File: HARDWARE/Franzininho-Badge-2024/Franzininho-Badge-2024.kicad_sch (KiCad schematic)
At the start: 15 parts, among them SW1 SW_Push, U1 CH32V003F4P6

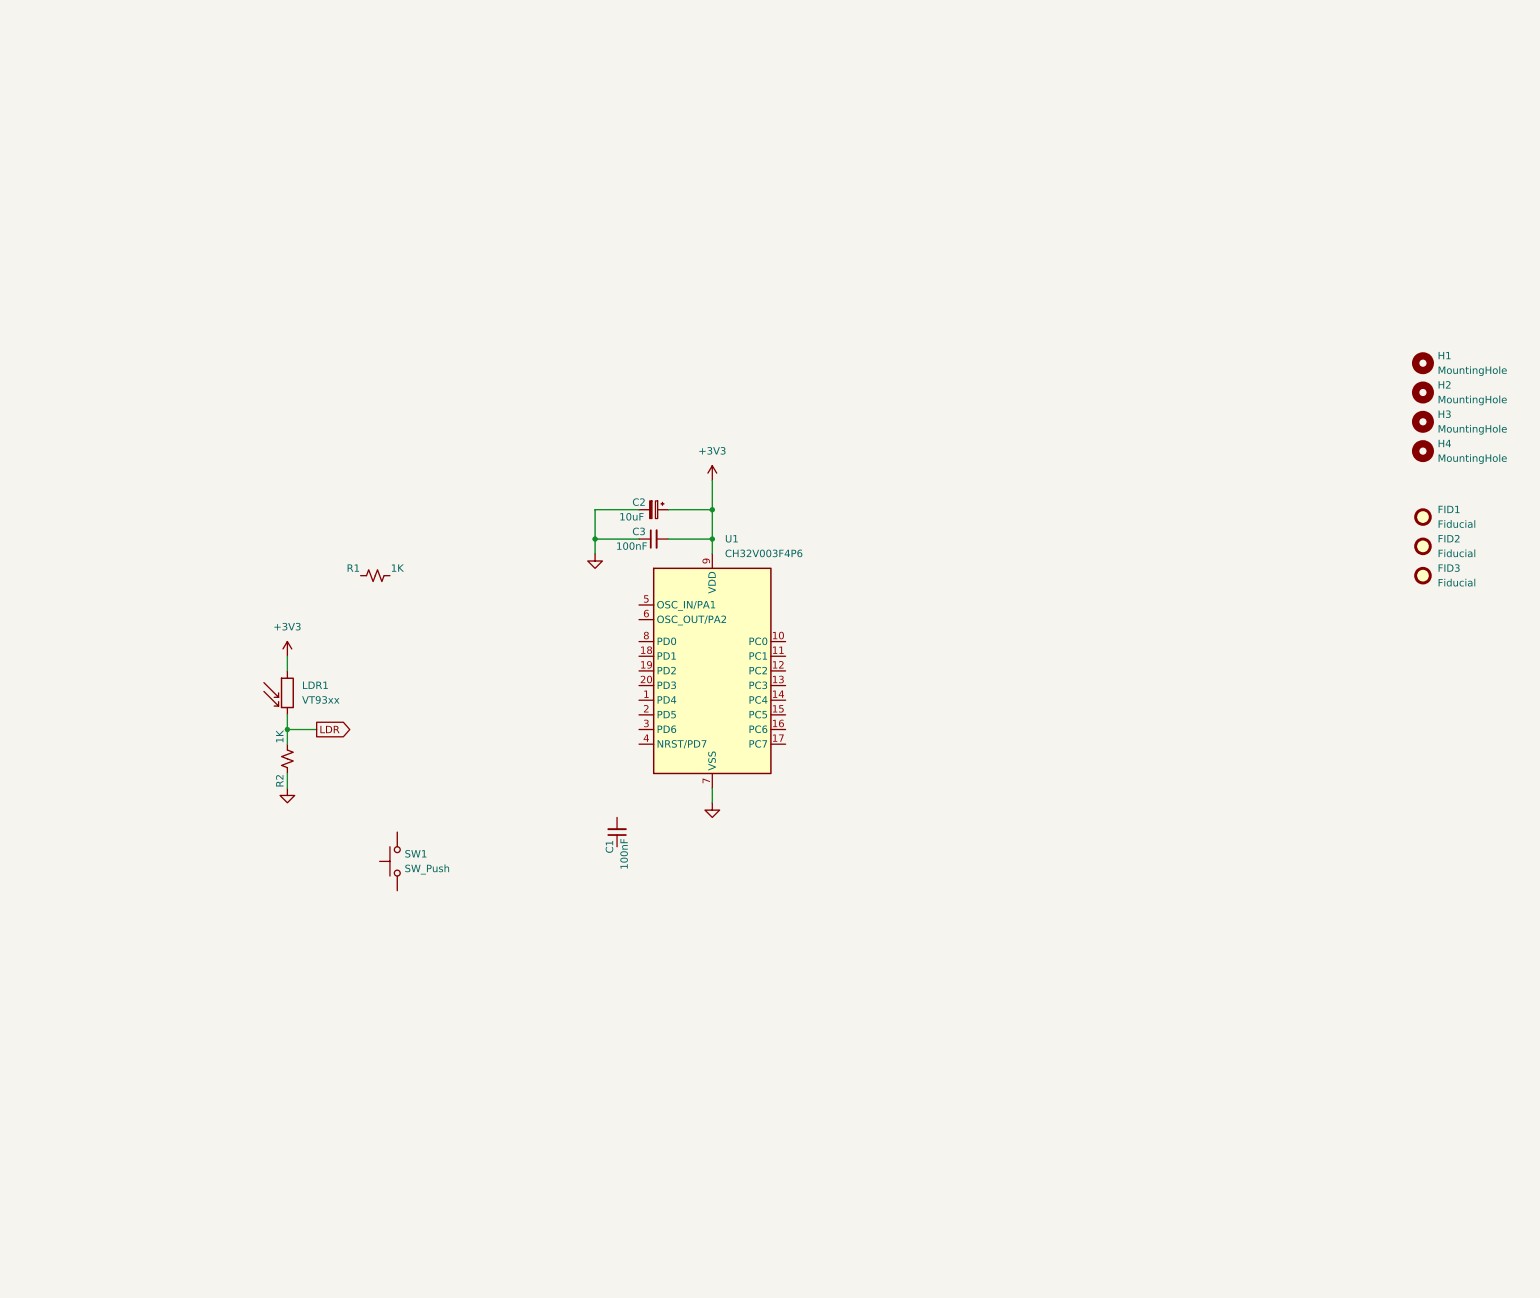
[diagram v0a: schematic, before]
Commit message: Adicionando displays.
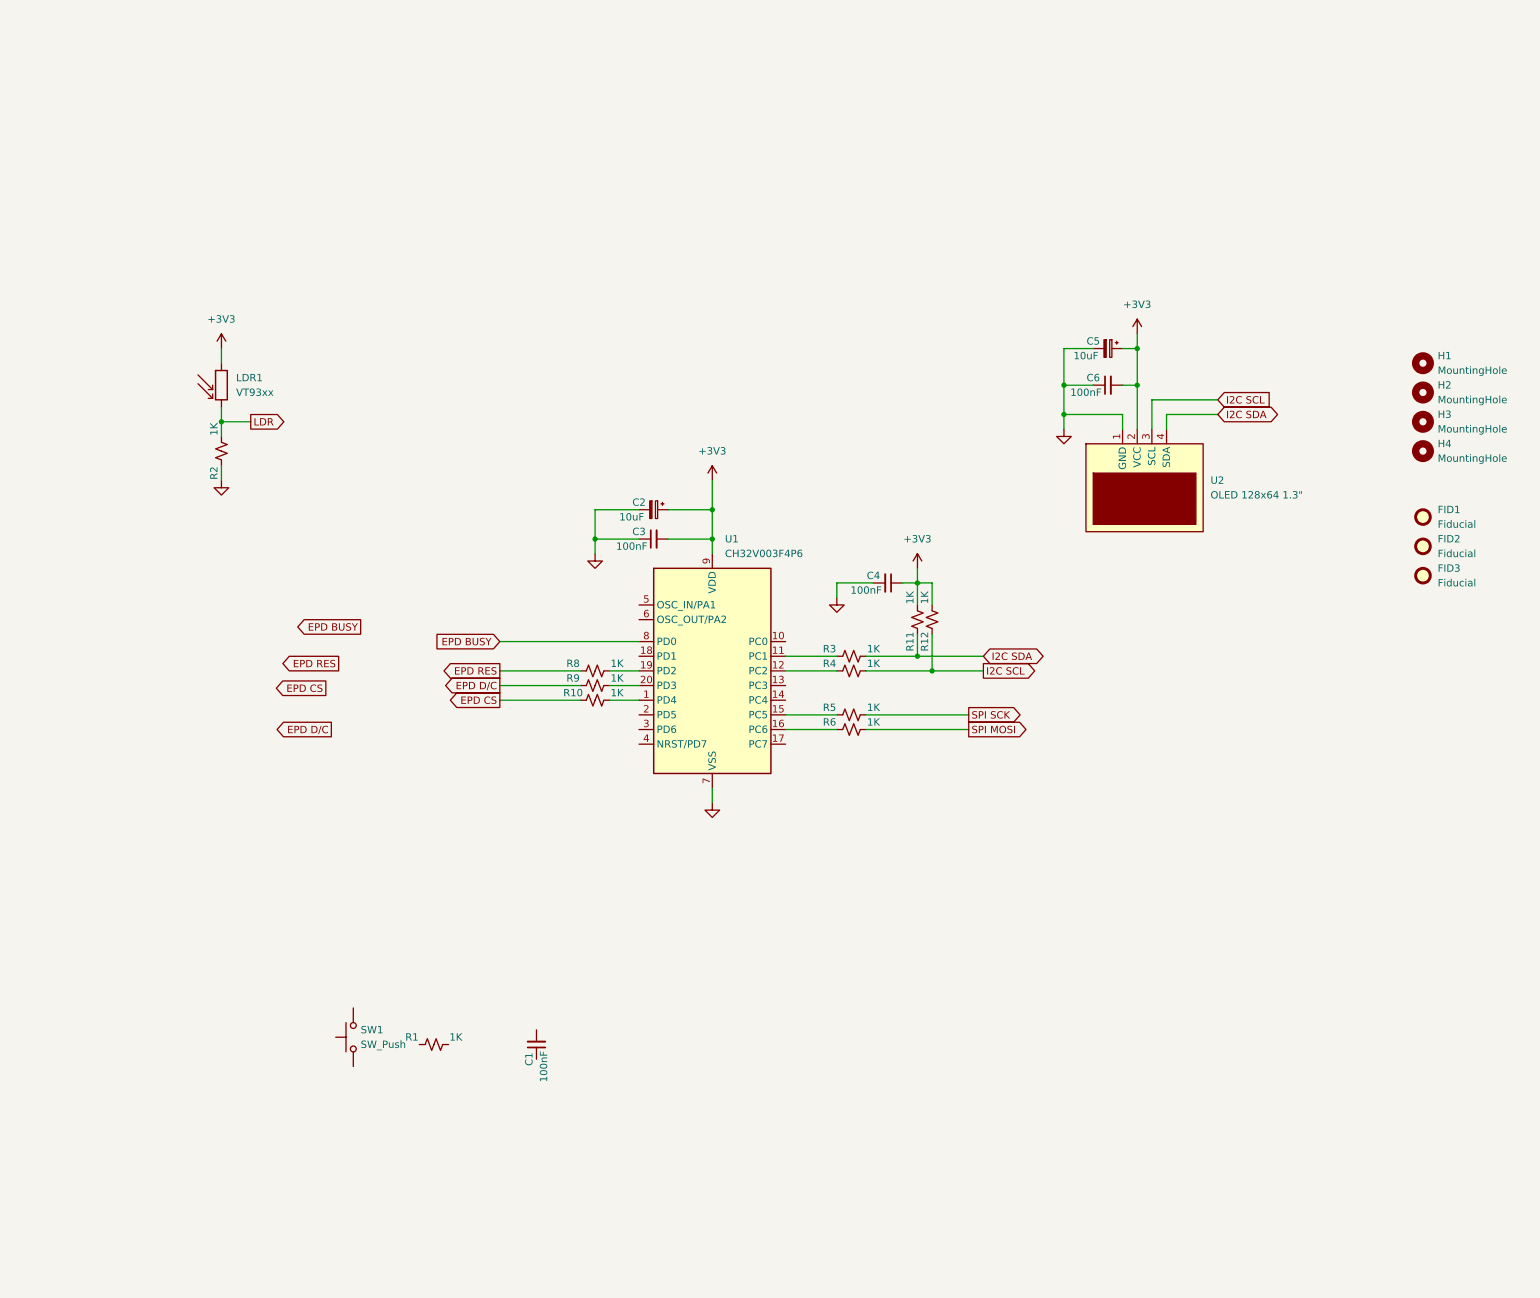
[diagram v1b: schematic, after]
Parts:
- added C4, C6: 100nF, Capacitor_SMD:C_0603_1608Metric_Pad1.08x0.95mm_HandSolder, symbol Device:C_Small
- added C5: 10uF, Capacitor_SMD:C_0805_2012Metric_Pad1.18x1.45mm_HandSolder, symbol Device:C_Polarized_Small
- added R10, R11, R12, R3, R4, R5, R6, R8, R9: 1K, Resistor_SMD:R_0603_1608Metric_Pad0.98x0.95mm_HandSolder, symbol Device:R_Small_US
- added U2: OLED 128x64 1.3", Franzininho-Badge:OLED 128x64 1.3in, symbol Franzininho-Badge:OLED_128x64_1.3{dblquote}
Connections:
- net +3V3: now also C4.1, C5.1, C6.2, R11.2, R12.2, U2.2 (VCC)
- net GND: now also C4.2, C5.2, C6.1, U2.1 (GND)
- net at U1.1 (PD4): now also R10.2
- net at U1.11 (PC1): now also R3.1
- net at U1.12 (PC2): now also R4.1
- net at U1.15 (PC5): now also R5.1
- net at U1.16 (PC6): now also R6.1
- net at U1.19 (PD2): now also R8.2
- net at U1.20 (PD3): now also R9.2
- net EPD BUSY: now reaches U1.8 (PD0)
- new net EPD CS: R10.1
- new net EPD D/C: R9.1
- new net EPD RES: R8.1
- new net I2C SCL: R12.1, R4.2, U2.3 (SCL)
- new net I2C SDA: R11.1, R3.2, U2.4 (SDA)
- new net SPI MOSI: R6.2
- new net SPI SCK: R5.2
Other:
- moved on the sheet: C1, LDR1, R1, R2, SW1

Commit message: Esboço inicial do layout.
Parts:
- added J1: Conn_01x03_Pin, Connector_PinHeader_2.54mm:PinHeader_1x03_P2.54mm_Horizontal, symbol Connector:Conn_01x03_Pin
- added J2: Conn_01x04_Pin, Connector_PinHeader_2.54mm:PinHeader_1x04_P2.54mm_Horizontal, symbol Connector:Conn_01x04_Pin
- added R13, R7: 1K, Resistor_SMD:R_0603_1608Metric_Pad0.98x0.95mm_HandSolder, symbol Device:R_Small_US
- added U3: ~, Franzininho-Badge:EPAPER_1.54in_200x200, symbol Franzininho-Badge:EPAPER_1.54in_200x200
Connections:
- net +3V3: now also J1.1 (Pin_1), J2.1 (Pin_1), U3.8 (VCC)
- net EPD BUSY: now also U3.1 (BUSY)
- net EPD CS: now also U3.4 (CS)
- net EPD D/C: now also U3.3 (D/C)
- net EPD RES: now also U3.2 (RES)
- net GND: now also J1.3 (Pin_3), J2.4 (Pin_4), U3.7 (GND)
- net SPI MOSI: now also U3.6 (SDA)
- net SPI SCK: now also U3.5 (SCL)
- net at U1.18 (PD1): now also R7.2
- net at U1.2 (PD5): now also R13.2
- net MCU RX: now reaches U1.3 (PD6)
- net MCU RX: now also J2.2 (Pin_2)
- new net MCU TX: J2.3 (Pin_3), R13.1
- new net SWIO: J1.2 (Pin_2), R7.1

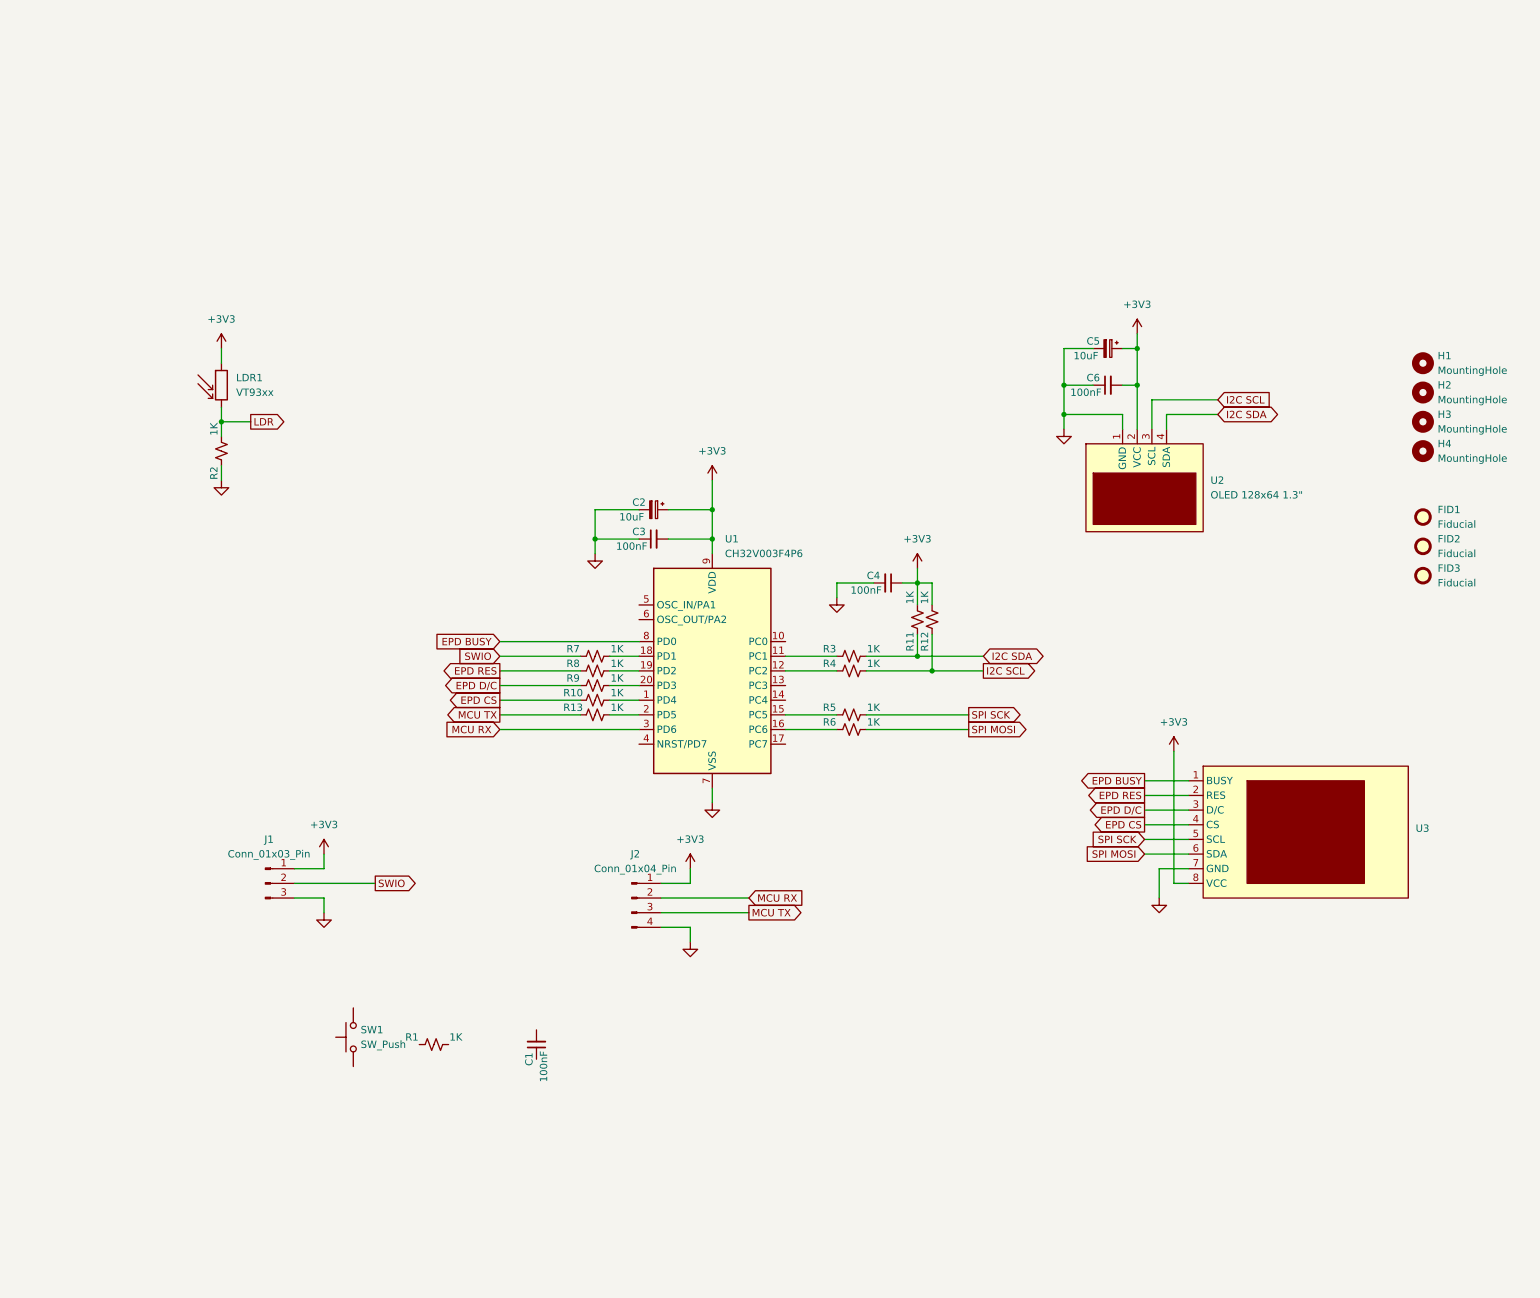
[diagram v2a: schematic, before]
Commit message: Adicionado display de 2.13in; continuação do layout.
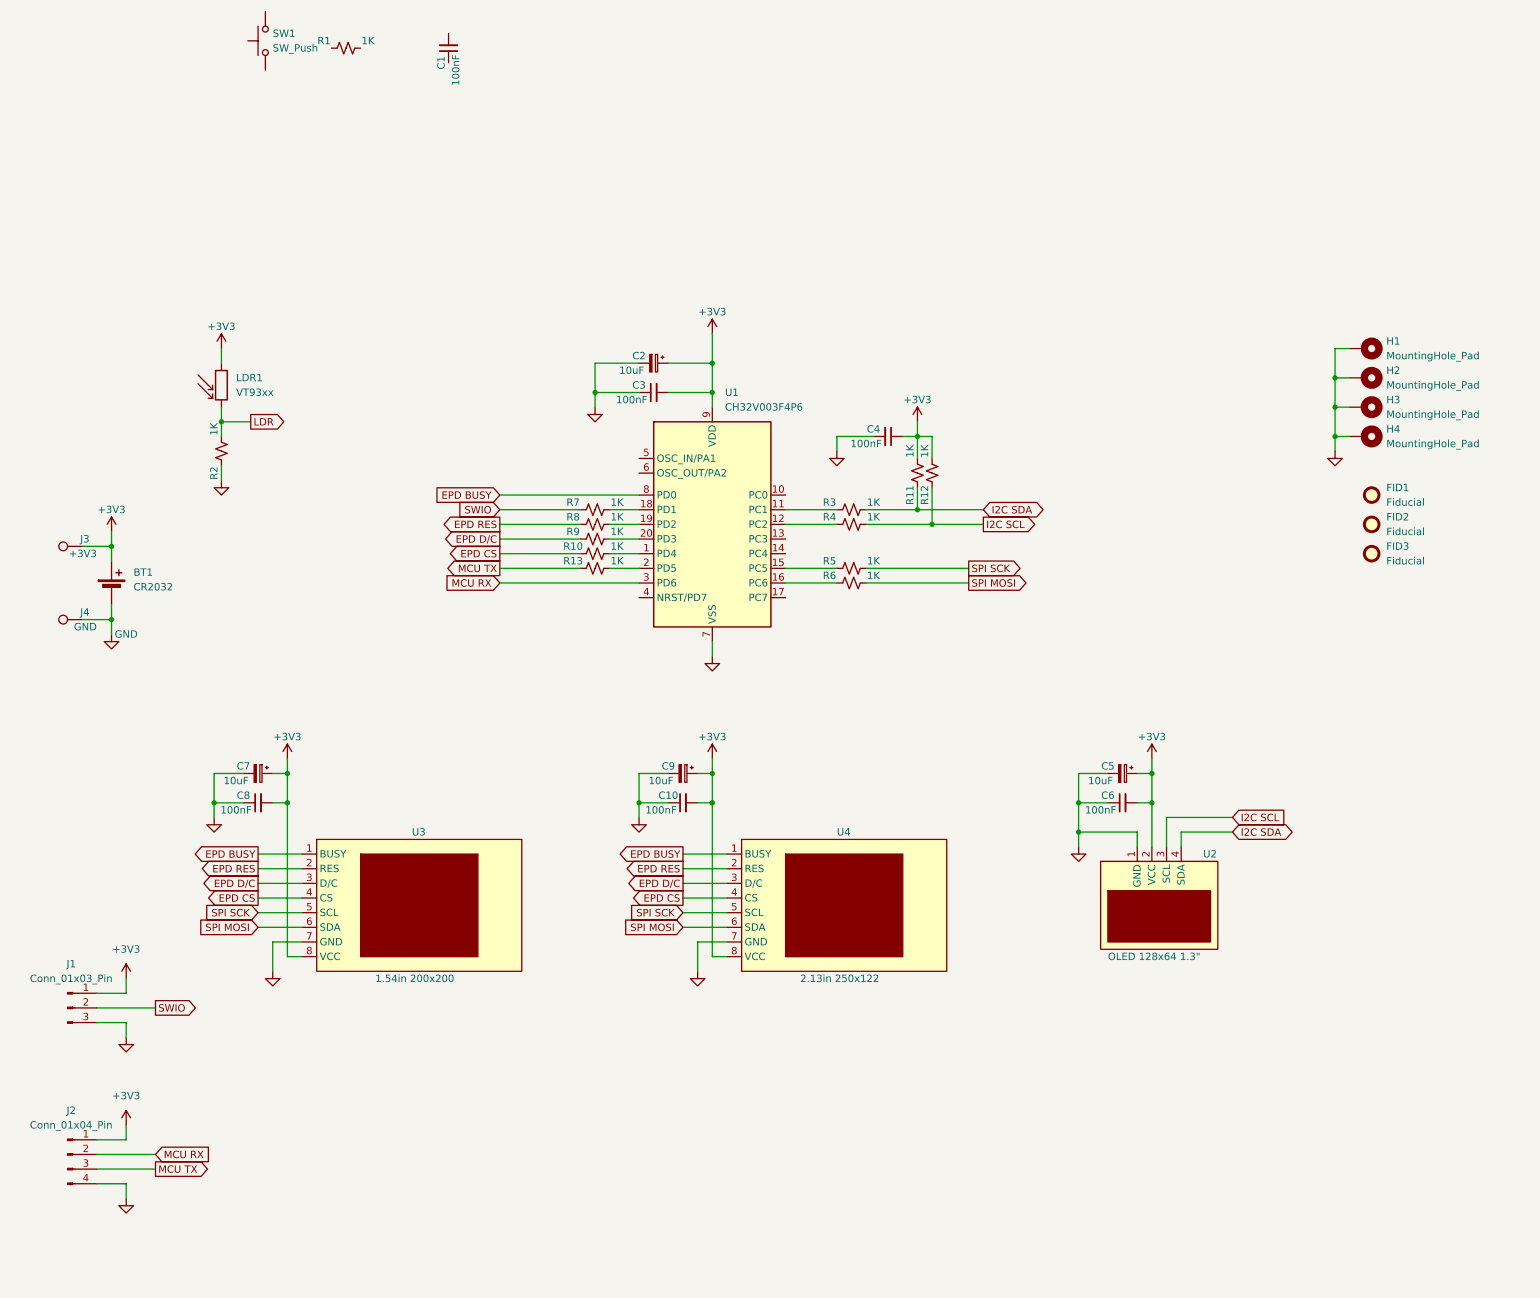
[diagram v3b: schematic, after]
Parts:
- removed H1, H2, H3, H4: MountingHole, MountingHole:MountingHole_3.2mm_M3_ISO7380, symbol Mechanical:MountingHole
- added BT1: CR2032, Battery:BatteryHolder_Keystone_3002_1x2032, symbol Device:Battery_Cell
- added C10, C8: 100nF, Capacitor_SMD:C_0603_1608Metric_Pad1.08x0.95mm_HandSolder, symbol Device:C_Small
- added C7, C9: 10uF, Capacitor_SMD:C_0805_2012Metric_Pad1.18x1.45mm_HandSolder, symbol Device:C_Polarized_Small
- added H1, H2, H3, H4: MountingHole_Pad, MountingHole:MountingHole_3.2mm_M3_Pad, symbol Mechanical:MountingHole_Pad
- added J3: +3V3, TestPoint:TestPoint_THTPad_D1.5mm_Drill0.7mm, symbol Connector:TestPoint
- added J4: GND, TestPoint:TestPoint_THTPad_D1.5mm_Drill0.7mm, symbol Connector:TestPoint
- added U4: 2.13in 250x122, Franzininho-Badge:EPAPER_2.13in_250x122, symbol Franzininho-Badge:EPAPER_2.13in_250x122
- U3: value ~ -> 1.54in 200x200
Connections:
- net +3V3: now also BT1.1 (+), C10.2, C7.1, C8.2, C9.1, J3.1, U4.8 (VCC)
- net EPD BUSY: now also U4.1 (BUSY)
- net EPD CS: now also U4.4 (CS)
- net EPD D/C: now also U4.3 (D/C)
- net EPD RES: now also U4.2 (RES)
- net GND: now also BT1.2 (-), C10.1, C7.2, C8.1, C9.2, H1.1, H2.1, H3.1, H4.1, J4.1, U4.7 (GND)
- net SPI MOSI: now also U4.6 (SDA)
- net SPI SCK: now also U4.5 (SCL)
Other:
- moved on the sheet: C1, C2, C3, C4, C5, C6, FID1, FID2, FID3, J1, J2, R1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

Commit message: Adicionado circuito liga-desliga; finalizando layout.
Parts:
- removed C1: 100nF, Capacitor_SMD:C_0603_1608Metric_Pad1.08x0.95mm_HandSolder, symbol Device:C_Small
- removed LDR1: VT93xx, OptoDevice:R_LDR_4.9x4.2mm_P2.54mm_Vertical, symbol Sensor_Optical:VT93xx
- removed R2: 1K, Resistor_SMD:R_0603_1608Metric_Pad0.98x0.95mm_HandSolder, symbol Device:R_Small_US
- added C12: 100nF, Capacitor_SMD:C_0603_1608Metric_Pad1.08x0.95mm_HandSolder, symbol Device:C_Small
- added C3: 10uF, Capacitor_SMD:C_0805_2012Metric_Pad1.18x1.45mm_HandSolder, symbol Device:C_Polarized_Small
- added Q1: SIL2308, Package_TO_SOT_SMD:SOT-23-6_Handsoldering, symbol Franzininho-Badge:SIL2308
- added R15: 1K, Resistor_SMD:R_0603_1608Metric_Pad0.98x0.95mm_HandSolder, symbol Device:R_Small_US
- added R16, R17: 100K, Resistor_SMD:R_0603_1608Metric_Pad0.98x0.95mm_HandSolder, symbol Device:R_Small_US
- added SW2: USER, Button_Switch_SMD:SW_Push_1P1T_NO_CK_KSC6xxJ, symbol Switch:SW_Push
- added SW3: RESET, Button_Switch_SMD:SW_Push_1P1T_NO_CK_KSC6xxJ, symbol Switch:SW_Push
- added TP3: +3V, TestPoint:TestPoint_THTPad_D1.5mm_Drill0.7mm, symbol Connector:TestPoint
- R1: value 1K -> 100K
- SW1: value SW_Push -> ON/OFF
- TP1: renamed from J3; value +3V3 -> +VBAT
- renumbered C7 to C1, C5 to C10, C6 to C11, C8 to C2, C2 to C5, C3 to C6, C9 to C7, C10 to C8, C4 to C9, R4 to R10, R5 to R11, R6 to R12, R11 to R13, R12 to R14, R7 to R4, R8 to R5, R9 to R6, R10 to R7, R13 to R8, R3 to R9, J4 to TP2, U3 to U1, U1 to U2, U4 to U3, U2 to U4
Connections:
- net GND: now also SW1.1, C12.1, C3.2, Q1.5 (S1), SW2.1, SW3.1
- net MCU I2C SCL: now reaches R10.1, U2.12 (PC2)
- net MCU UART TX: now reaches R8.2, U2.2 (PD5)
- net at SW1.2: now also R1.1, Q1.3 (G2), Q1.6 (D1)
- net MCU SPI MOSI: now reaches R12.1, U2.16 (PC6)
- net MCU EPD D/~{C}: now reaches R6.2, U2.20 (PD3)
- net +VBAT: now reaches R1.2
- net +VBAT: now also BT1.1 (+), TP1.1, Q1.2 (S2)
- net MCU SPI SCK: now reaches R11.1, U2.15 (PC5)
- net MCU I2C SDA: now reaches R9.1, U2.11 (PC1)
- net MCU EPD  RES: now reaches R5.2, U2.19 (PD2)
- net MCU SPI ~{CS}: now reaches R7.2, U2.1 (PD4)
- net at U2.10 (PC0): now also R15.1
- net USER BUTTON: now reaches U2.13 (PC3)
- net USER BUTTON: now also R16.1, SW2.2
- net ~{RESET}: now reaches U2.4 (NRST/PD7)
- net ~{RESET}: now also C12.2, R17.1, SW3.2
- net +3V3 renamed +3V
- net +3V: now also C3.1, Q1.4 (D2), R16.2, R17.2, TP3.1; no longer BT1.1 (+), TP1.1
- net MCU RX renamed UART RX
- net MCU TX renamed UART TX
- new net ~{SHUTDOWN}: Q1.1 (G1), R15.2
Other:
- moved on the sheet: C9, R10, R11, R12, R13, R14, R4, R5, R6, R7, R8, R9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
